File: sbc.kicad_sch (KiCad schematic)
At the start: 0 parts

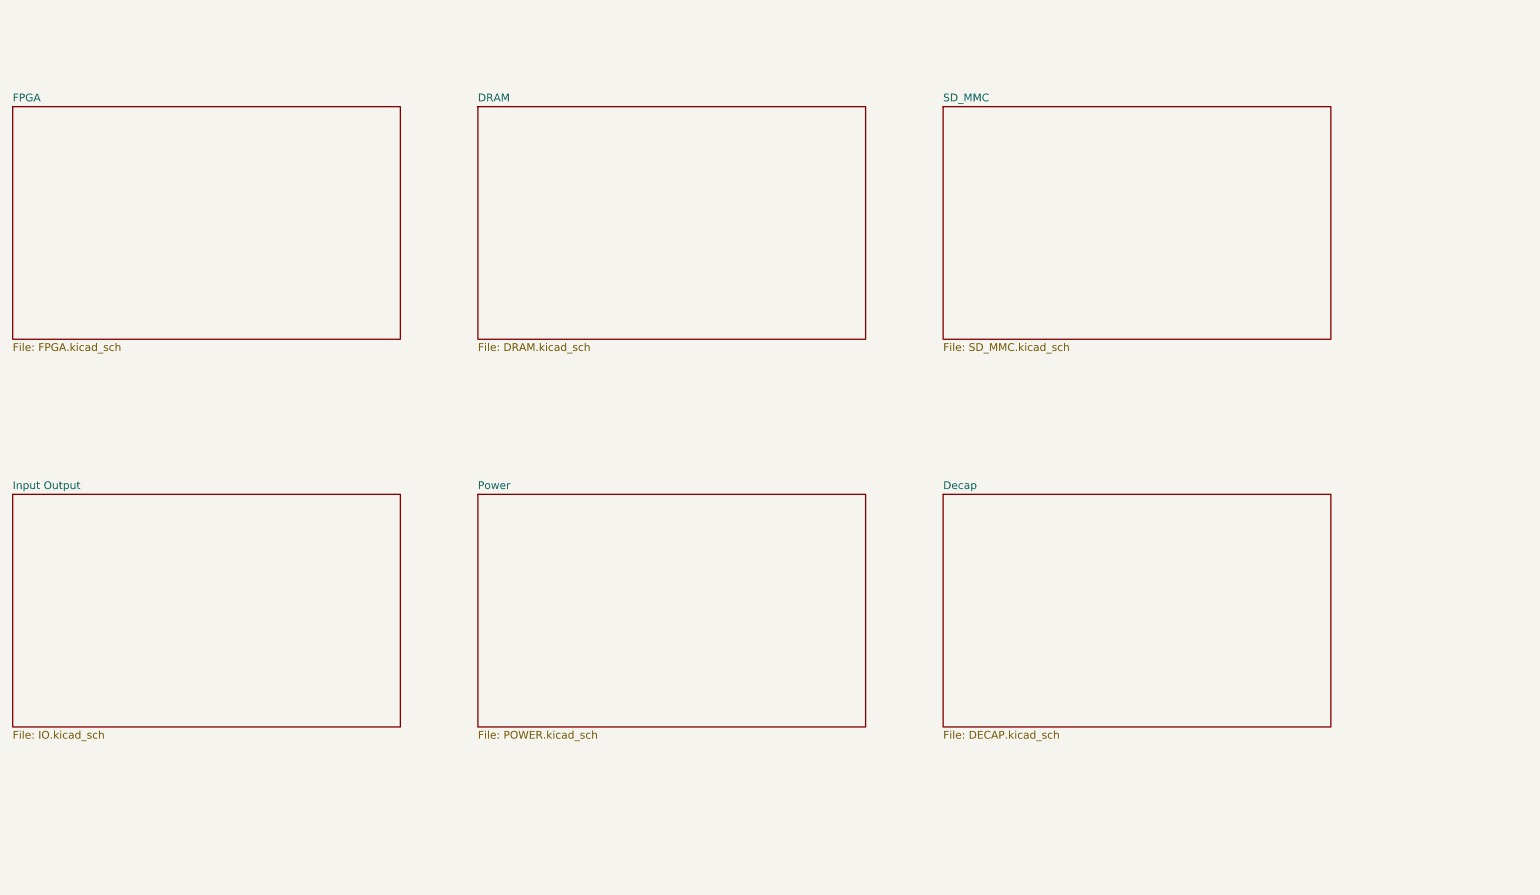
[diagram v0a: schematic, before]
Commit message: Changed power regulators, filled out DRAM, begin changing FPGA from ECP5 to ICE40
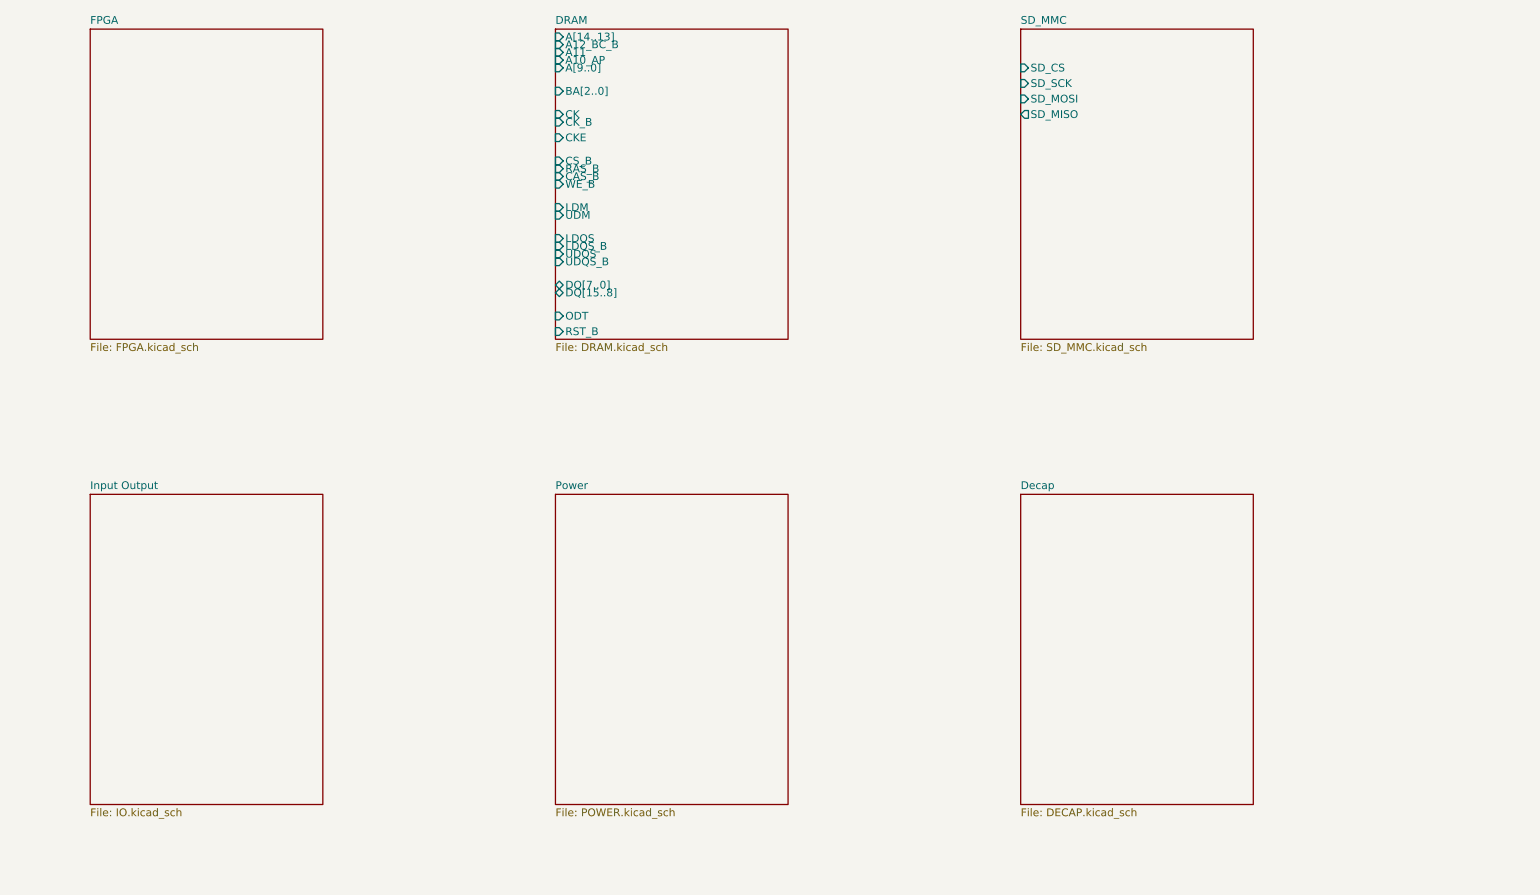
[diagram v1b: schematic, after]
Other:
- sheet DRAM ports: added A10_AP, A11, A12_BC_B, A[14..13], A[9..0], BA[2..0], CAS_B, CK, CKE, CK_B, CS_B, DQ[15..8], DQ[7..0], LDM, LDQS, LDQS_B, ODT, RAS_B, RST_B, UDM, UDQS, UDQS_B, WE_B; removed none
- sheet SD_MMC ports: added SD_CS, SD_MISO, SD_MOSI, SD_SCK; removed none

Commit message: Saving before changing RAM from DDR3 to Parallel SDR SRAM
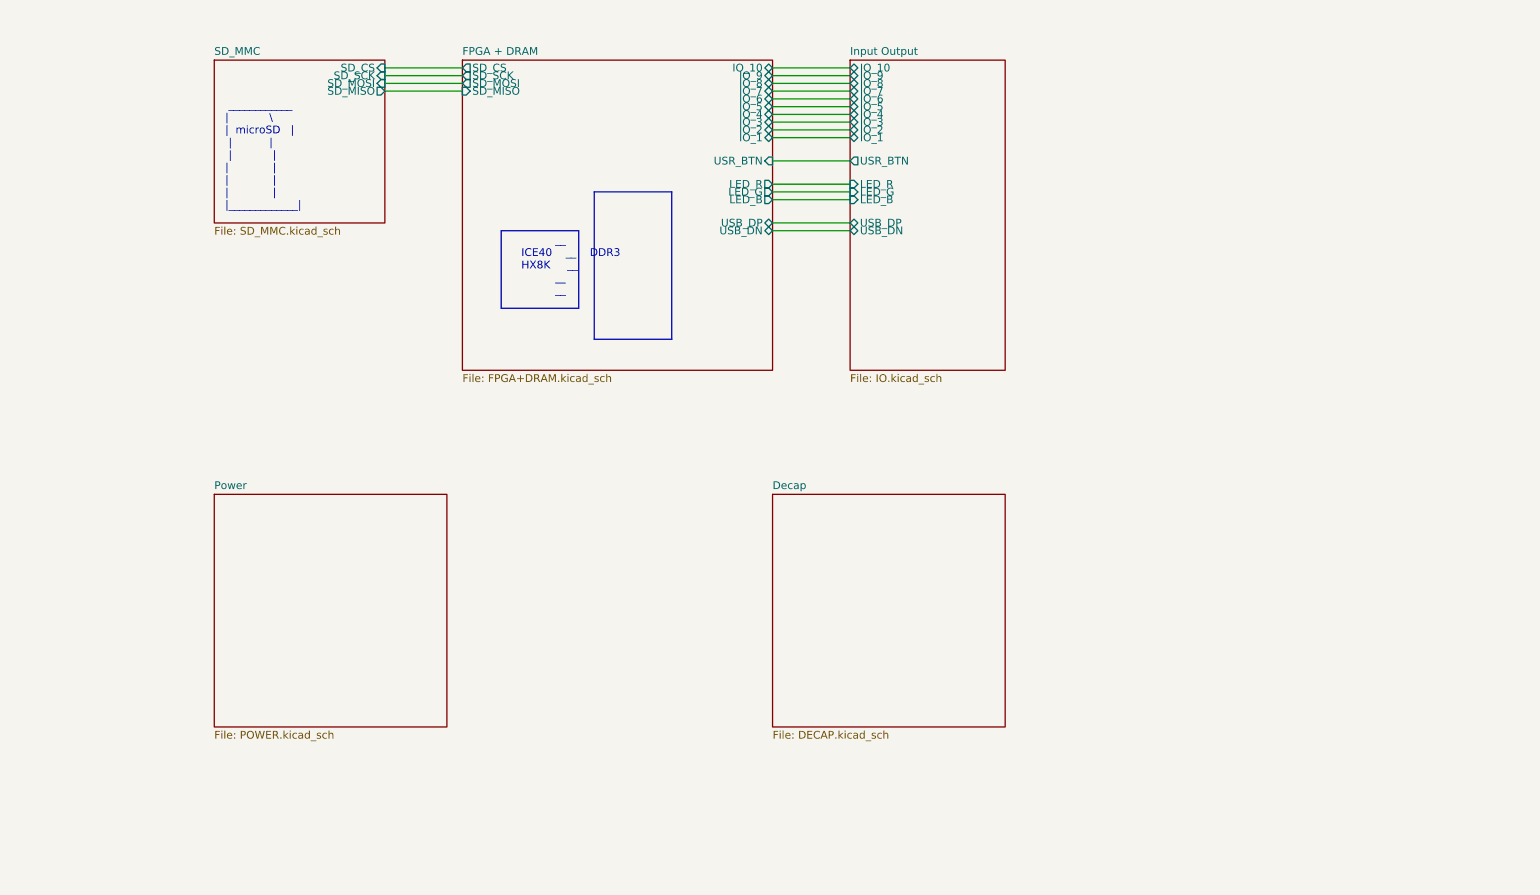
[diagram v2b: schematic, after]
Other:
- removed sheet DRAM
- removed sheet FPGA
- added sheet FPGA + DRAM (FPGA+DRAM.kicad_sch)
- sheet Input Output ports: added IO_1, IO_10, IO_2, IO_3, IO_4, IO_5, IO_6, IO_7, IO_8, IO_9, LED_B, LED_G, LED_R, USB_DN, USB_DP, USR_BTN; removed none
- note added: "__ ICE40 __ DDR3 HX8K __ __ __"
- note added: "____________ | \ | microSD | | | | | | | | | | | |_____________|"

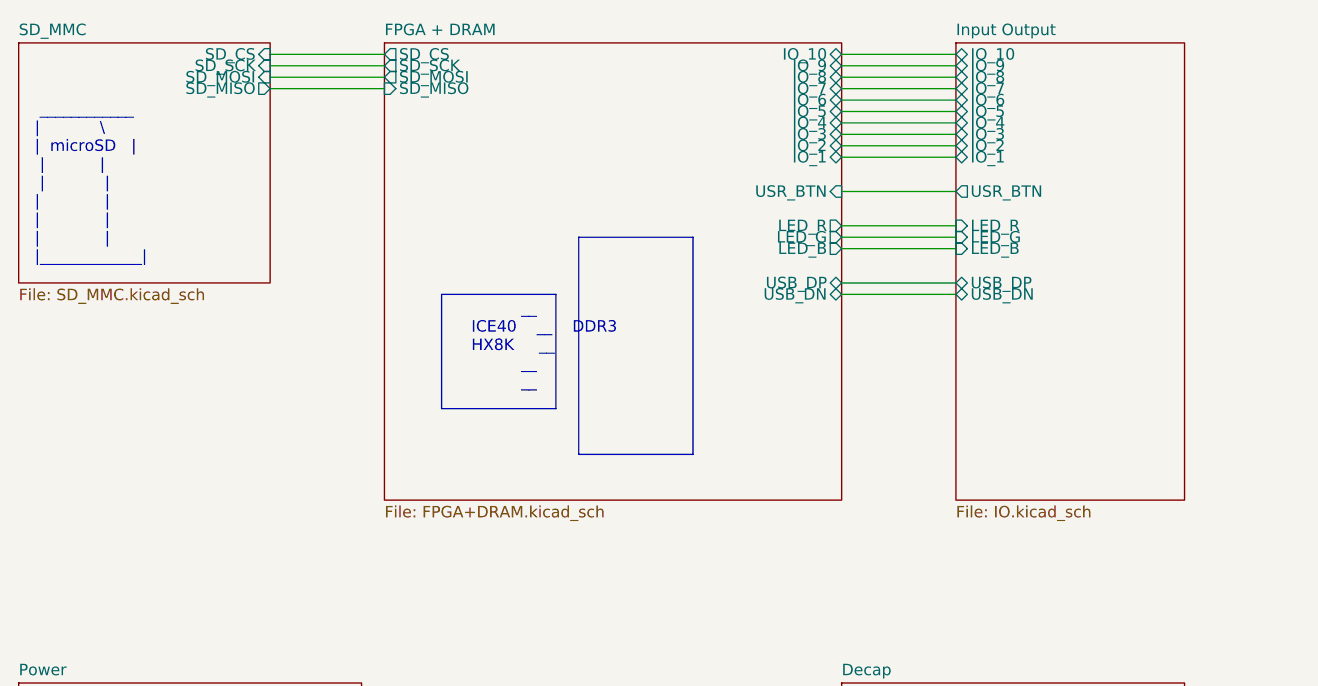
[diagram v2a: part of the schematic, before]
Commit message: Added more I/O. Changed power regulators
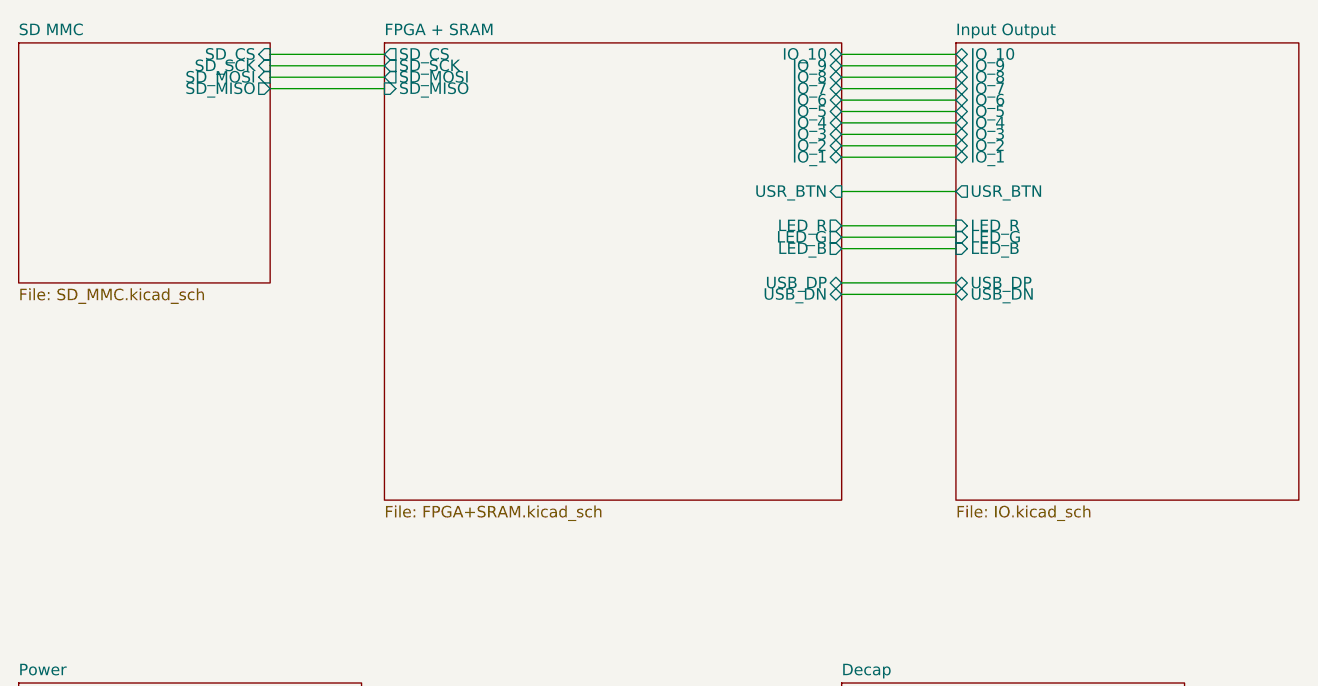
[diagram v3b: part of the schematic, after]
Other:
- sheet FPGA + DRAM renamed FPGA + SRAM
- sheet SD_MMC renamed SD MMC
- sheet FPGA + SRAM: file FPGA+DRAM.kicad_sch -> FPGA+SRAM.kicad_sch
- note removed: "__ ICE40 __ DDR3 HX8K __ __ __"
- note removed: "____________ | \ | microSD | | | | | | | | | | | |_____________|"

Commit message: Power routed. Saving before reworking ICE40 pins to optimize layout
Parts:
- added H1, H2, H3, H4: MountingHole, MountingHole:MountingHole_2.2mm_M2, symbol Mechanical:MountingHole
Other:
- added sheet USB (USB.kicad_sch)
- sheet FPGA + SRAM ports: added CDONE, FIFO[7..0], FIFO_RD_B, FIFO_RXF_B, FIFO_TXE_B, FIFO_WR_B, IO_B[10..1], IO_T[10..1], SD_CLK, SD_CMD, SD_DAT[3..0], SPI_CNFG_CS_B, SPI_CNFG_DI, SPI_CNFG_DO, SPI_CNFG_SCK, USB2_DN, USB2_DP, USB3_DN, USB3_DP, USR_BTN1; removed IO_1, IO_10, IO_2, IO_3, IO_4, IO_5, IO_6, IO_7, IO_8, IO_9, SD_CS, SD_MISO, SD_MOSI, SD_SCK, USB_DN, USB_DP, USR_BTN
- sheet Input Output ports: added CDONE, IO_B[10..1], IO_T[10..1], USR_BTN1; removed IO_1, IO_10, IO_2, IO_3, IO_4, IO_5, IO_6, IO_7, IO_8, IO_9, USB_DN, USB_DP, USR_BTN
- sheet SD MMC ports: added SD_CLK, SD_CMD, SD_DAT[3..0]; removed SD_CS, SD_MISO, SD_MOSI, SD_SCK
